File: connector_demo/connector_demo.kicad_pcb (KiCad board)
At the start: 2 copper layers, 81 x 29 mm, 4 parts, among them J1 PicoBlade 8-wide, J2 PicoLock 8-wide, J3 MicroLock

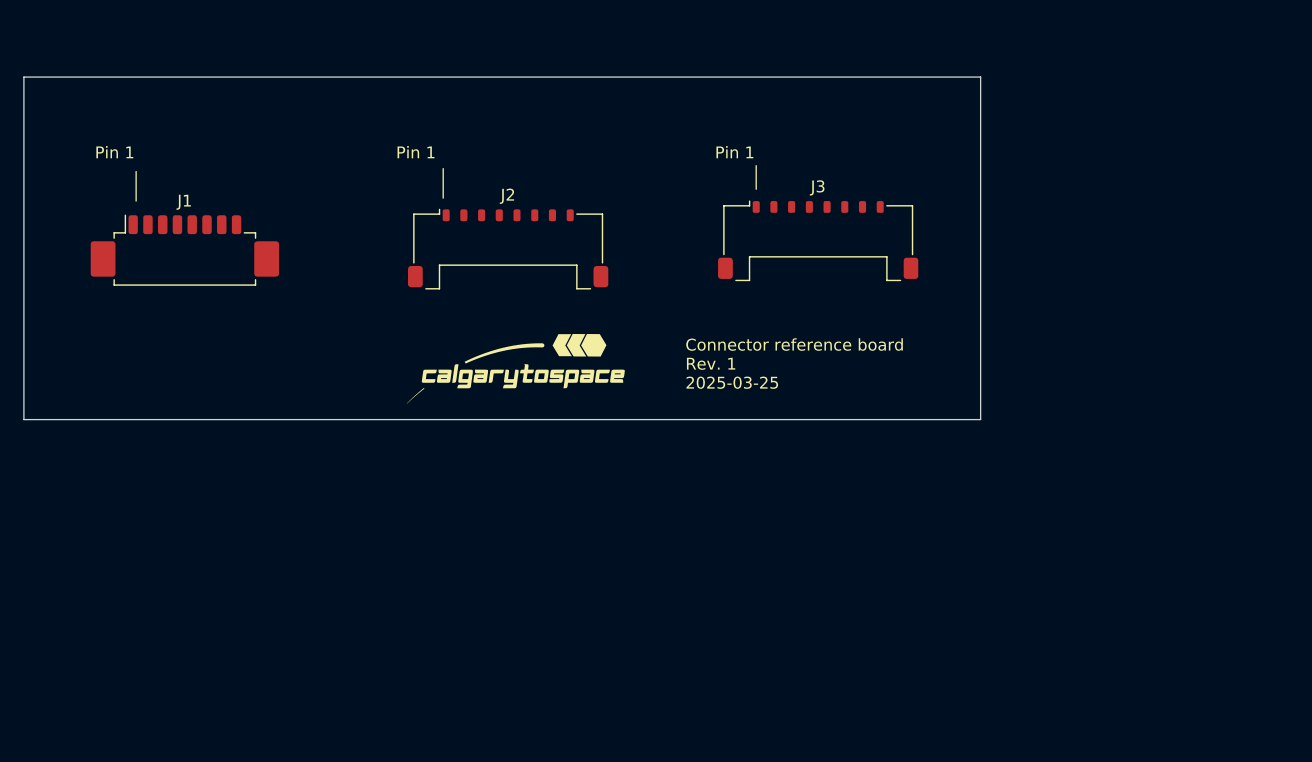
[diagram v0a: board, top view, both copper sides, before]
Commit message: added connector names
still confirming pin 1
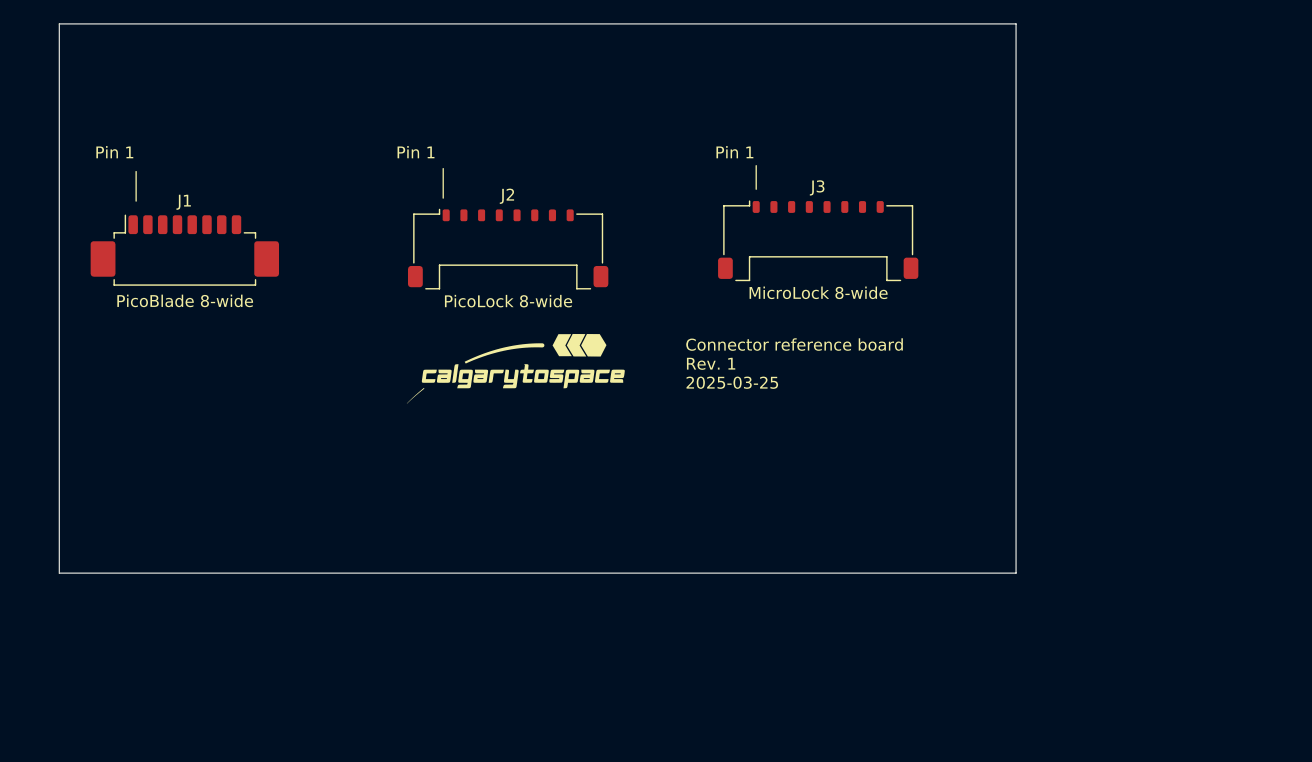
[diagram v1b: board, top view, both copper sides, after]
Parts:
- J3: value MicroLock -> MicroLock 8-wide
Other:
- board size 81 x 29 mm -> 81 x 46.5 mm
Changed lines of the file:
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@@
 		(property "Value" "PicoLock 8-wide"
 			(at 0 4.52 0)
-			(layer "F.Fab")
+			(layer "F.SilkS")
 			(effects
 				(font
@@
 			)
 		)
-		(property "Value" "MicroLock"
+		(property "Value" "MicroLock 8-wide"
 			(at 0 4.52 0)
-			(layer "F.Fab")
+			(layer "F.SilkS")
 			(effects
 				(font
@@
 		)
 		(property "Value" "PicoBlade 8-wide"
-			(at 0 3.8 0)
-			(layer "F.Fab")
+			(at 0 4.1 0)
+			(layer "F.SilkS")
 			(effects
 				(font
@@
 	)
 	(gr_rect
-		(start 89.5 63)
-		(end 170.5 92)
+		(start 92.5 58.5)
+		(end 173.5 105)
 		(stroke
 			(width 0.05)

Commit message: confirmed pin 1
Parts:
- moved G*** 2.06 mm to (130.5, 89.5)
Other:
- board text added: "Connector reference board Rev. 1 2025-03-30"
- board text removed: "Connector reference board Rev. 1 2025-03-25"
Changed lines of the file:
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@@
 	(footprint "logo:ctslogo1x2cm"
 		(layer "F.Cu")
-		(at 131 87.5)
+		(at 130.5 89.5)
 		(property "Reference" "G***"
 			(at -2.5 -2 0)
@@
 	)
 	(gr_line
-		(start 151.5 72.5)
-		(end 151.5 70.5)
+		(start 162 72.5)
+		(end 162 70.5)
 		(stroke
 			(width 0.1)
@@
 	)
 	(gr_text "Pin 1"
-		(at 148 70 0)
+		(at 161 70 0)
 		(layer "F.SilkS")
 		(effects
@@
 		)
 	)
-	(gr_text "Connector reference board\nRev. 1 \n2025-03-25"
-		(at 145.5 89.5 0)
+	(gr_text "Connector reference board\nRev. 1 \n2025-03-30"
+		(at 145.5 92.5 0)
 		(layer "F.SilkS")
 		(effects

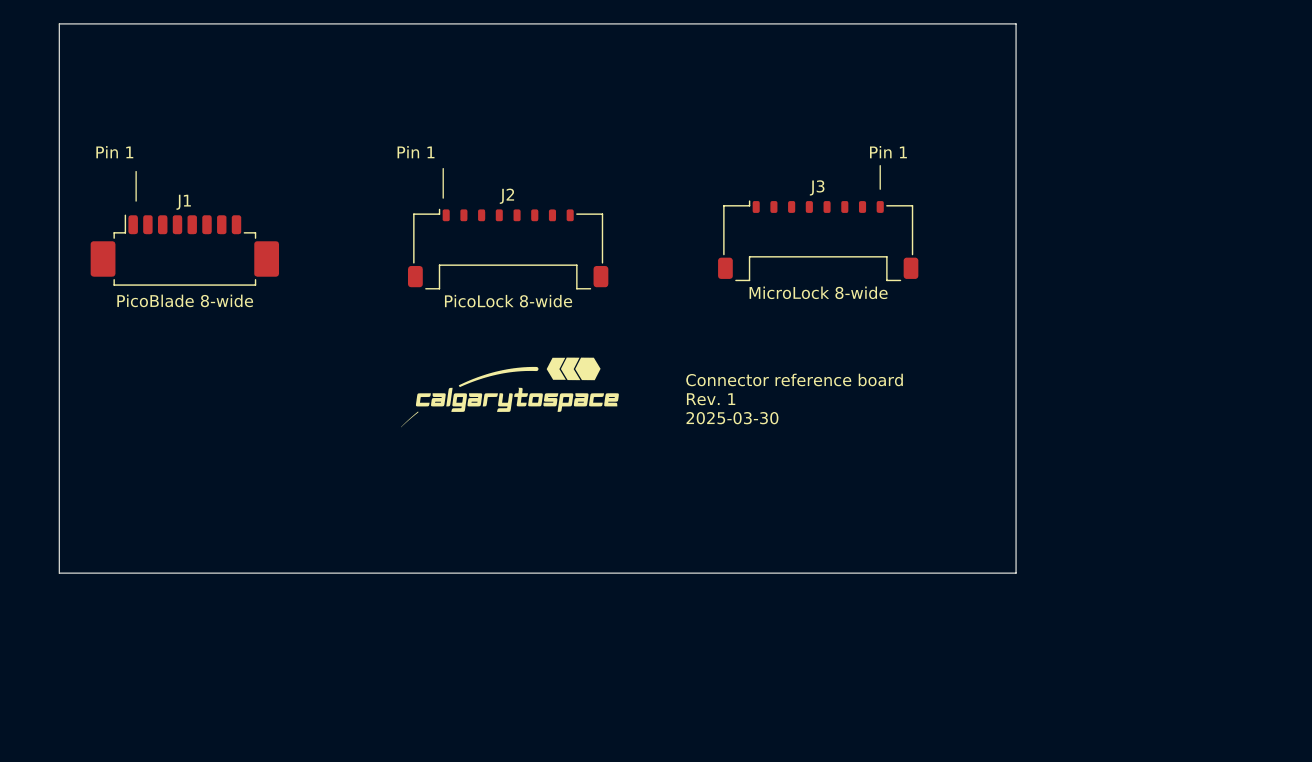
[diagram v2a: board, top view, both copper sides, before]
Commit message: added header pins and traces
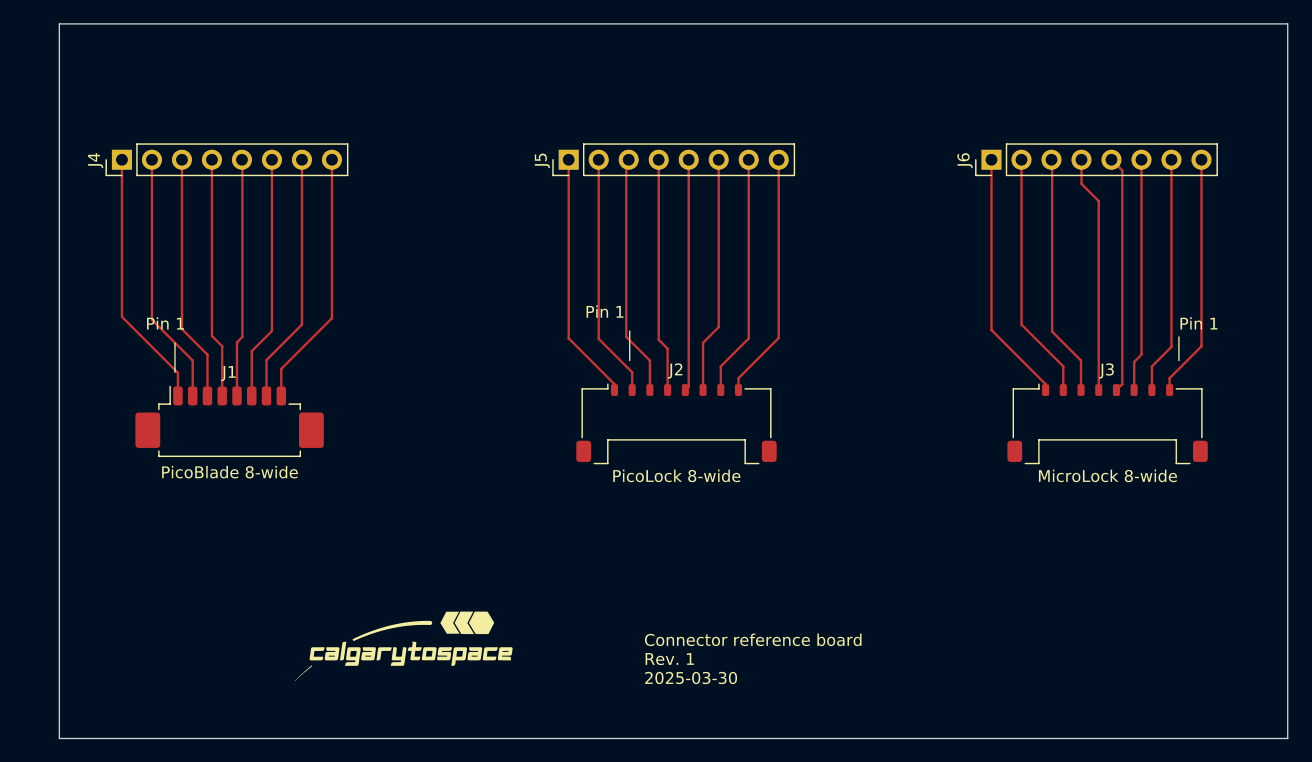
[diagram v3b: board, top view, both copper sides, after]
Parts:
- added J4: Conn_01x08_Pin, Connector_PinHeader_2.54mm:PinHeader_1x08_P2.54mm_Vertical, F.Cu at (97.8, 70.0)
- added J5: Conn_01x08_Pin, Connector_PinHeader_2.54mm:PinHeader_1x08_P2.54mm_Vertical, F.Cu at (135.6, 70.0)
- added J6: Conn_01x08_Pin, Connector_PinHeader_2.54mm:PinHeader_1x08_P2.54mm_Vertical, F.Cu at (171.4, 70.0)
- moved J3 29.0 mm to (181.2, 92.3)
- moved G*** 23.3 mm to (121.5, 111.0)
- moved J2 20.5 mm to (144.8, 92.3)
- moved J1 15.0 mm to (106.9, 92.4)
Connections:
- J1 pad 1: unconnected-(J1-Pin_1-Pad1) -> Net-(J1-Pin_1)
- J1 pad 2: unconnected-(J1-Pin_2-Pad2) -> Net-(J1-Pin_2)
- J1 pad 3: unconnected-(J1-Pin_3-Pad3) -> Net-(J1-Pin_3)
- J1 pad 4: unconnected-(J1-Pin_4-Pad4) -> Net-(J1-Pin_4)
- J1 pad 5: unconnected-(J1-Pin_5-Pad5) -> Net-(J1-Pin_5)
- J1 pad 6: unconnected-(J1-Pin_6-Pad6) -> Net-(J1-Pin_6)
- J1 pad 7: unconnected-(J1-Pin_7-Pad7) -> Net-(J1-Pin_7)
- J1 pad 8: unconnected-(J1-Pin_8-Pad8) -> Net-(J1-Pin_8)
- J2 pad 1: unconnected-(J2-Pin_1-Pad1) -> Net-(J2-Pin_1)
- J2 pad 2: unconnected-(J2-Pin_2-Pad2) -> Net-(J2-Pin_2)
- J2 pad 3: unconnected-(J2-Pin_3-Pad3) -> Net-(J2-Pin_3)
- J2 pad 4: unconnected-(J2-Pin_4-Pad4) -> Net-(J2-Pin_4)
- J2 pad 5: unconnected-(J2-Pin_5-Pad5) -> Net-(J2-Pin_5)
- J2 pad 6: unconnected-(J2-Pin_6-Pad6) -> Net-(J2-Pin_6)
- J2 pad 7: unconnected-(J2-Pin_7-Pad7) -> Net-(J2-Pin_7)
- J2 pad 8: unconnected-(J2-Pin_8-Pad8) -> Net-(J2-Pin_8)
- J3 pad 1: unconnected-(J3-Pin_1-Pad1) -> Net-(J3-Pin_1)
- J3 pad 2: unconnected-(J3-Pin_2-Pad2) -> Net-(J3-Pin_2)
- J3 pad 3: unconnected-(J3-Pin_3-Pad3) -> Net-(J3-Pin_3)
- J3 pad 4: unconnected-(J3-Pin_4-Pad4) -> Net-(J3-Pin_4)
- J3 pad 5: unconnected-(J3-Pin_5-Pad5) -> Net-(J3-Pin_5)
- J3 pad 6: unconnected-(J3-Pin_6-Pad6) -> Net-(J3-Pin_6)
- J3 pad 7: unconnected-(J3-Pin_7-Pad7) -> Net-(J3-Pin_7)
- J3 pad 8: unconnected-(J3-Pin_8-Pad8) -> Net-(J3-Pin_8)
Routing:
- net Net-(J1-Pin_1): track 0.00 -> 22.0 mm
- net Net-(J1-Pin_8): track 0.00 -> 21.8 mm
- net Net-(J1-Pin_2): track 0.00 -> 21.4 mm
- net Net-(J3-Pin_1): track 0.00 -> 21.4 mm
- net Net-(J1-Pin_7): track 0.00 -> 21.2 mm
- net Net-(J2-Pin_1): track 0.00 -> 21.1 mm
- net Net-(J3-Pin_2): track 0.00 -> 21.0 mm
- net Net-(J2-Pin_8): track 0.00 -> 20.9 mm
- net Net-(J1-Pin_3): track 0.00 -> 20.9 mm
- net Net-(J1-Pin_6): track 0.00 -> 20.7 mm
- net Net-(J2-Pin_2): track 0.00 -> 20.7 mm
- net Net-(J3-Pin_8): track 0.00 -> 20.6 mm
- net Net-(J3-Pin_3): track 0.00 -> 20.5 mm
- net Net-(J2-Pin_7): track 0.00 -> 20.5 mm
- net Net-(J2-Pin_3): track 0.00 -> 20.4 mm
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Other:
- board size 81 x 46.5 mm -> 104 x 60.5 mm

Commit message: Fixed microlock connector, generated BOM
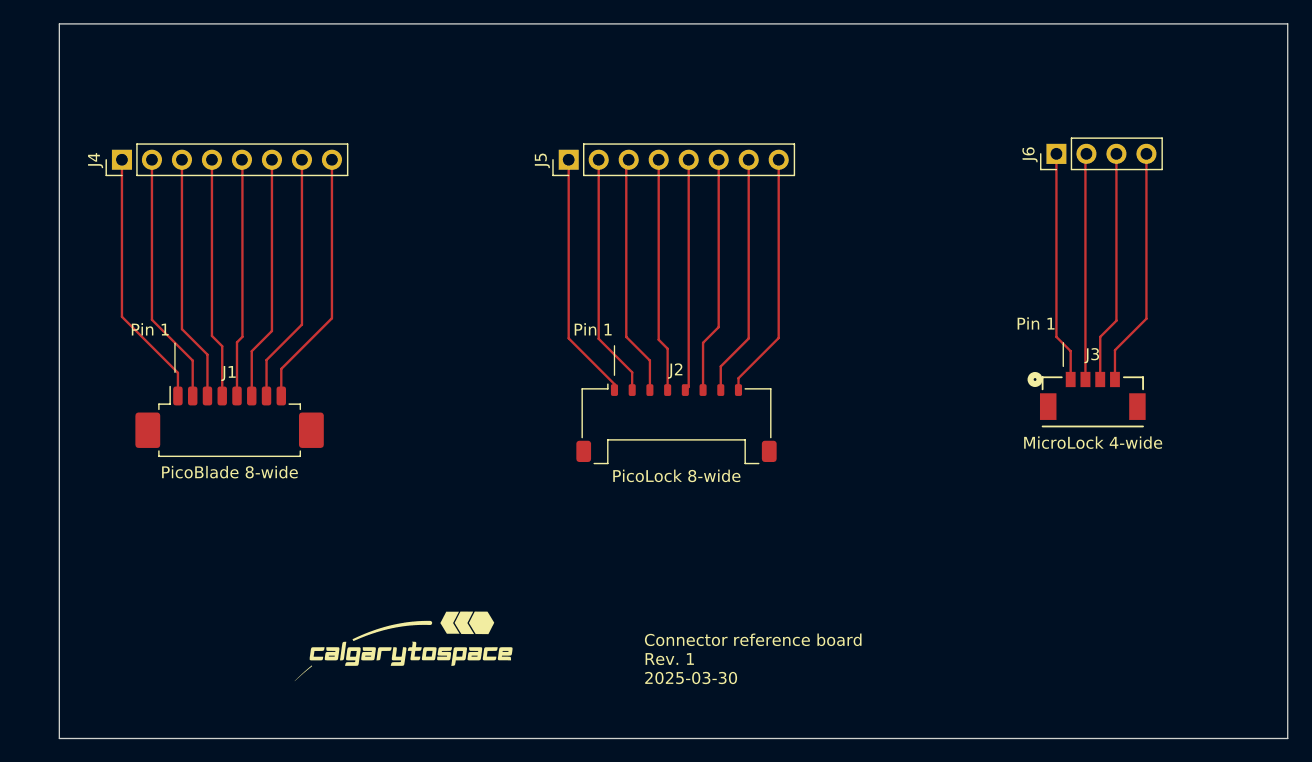
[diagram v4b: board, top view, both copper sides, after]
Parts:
- J3: value MicroLock 8-wide -> MicroLock 4-wide; footprint Connector_Molex:Molex_Pico-Lock_504050-0891_1x08-1MP_P1.50mm_Horizontal -> microlock:CONN04_5055670471_MOL
- J6: value Conn_01x08_Pin -> Conn_01x04_Pin; footprint Connector_PinHeader_2.54mm:PinHeader_1x08_P2.54mm_Vertical -> Connector_PinHeader_2.54mm:PinHeader_1x04_P2.54mm_Vertical
- moved J6 5.52 mm to (176.9, 69.5)
- moved J3 2.19 mm to (180.0, 90.5), turned to 180 degrees
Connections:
- J3 pad 5: Net-(J3-Pin_5) -> (no net)
- J3 pad 6: Net-(J3-Pin_6) -> (no net)
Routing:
- net Net-(J3-Pin_8): track 20.6 -> 0.00 mm
- net Net-(J3-Pin_7): track 20.2 -> 0.00 mm
- net Net-(J3-Pin_5): track 20.1 -> 0.00 mm
- net Net-(J3-Pin_6): track 19.8 -> 0.00 mm
- net Net-(J3-Pin_2): track 21.0 -> 19.1 mm
- net Net-(J3-Pin_1): track 21.4 -> 19.7 mm
- net Net-(J3-Pin_3): track 20.5 -> 19.7 mm
